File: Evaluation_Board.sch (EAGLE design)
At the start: 38 parts, among them IC1 MEGA32-A, IC2 FT232RL, IC3 317EMP, J1 DCJ0202, Q1 16 MHz

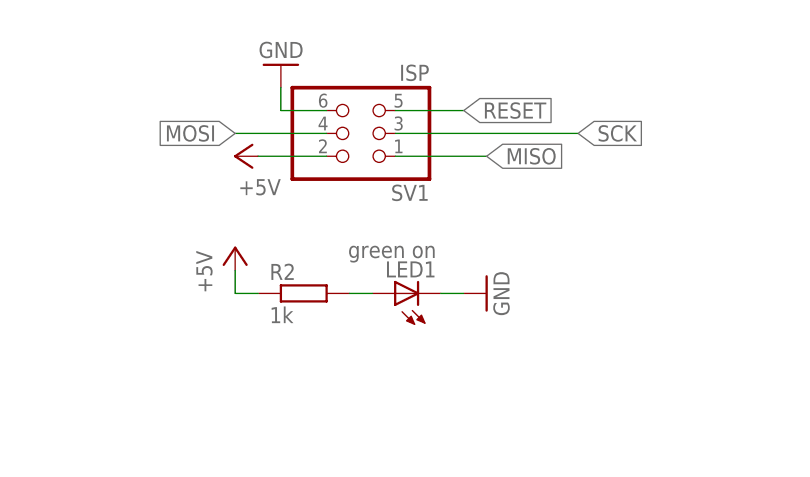
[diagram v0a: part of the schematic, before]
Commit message: Added name for ISP connector and placed a pin-one-marker on silk screen layer.
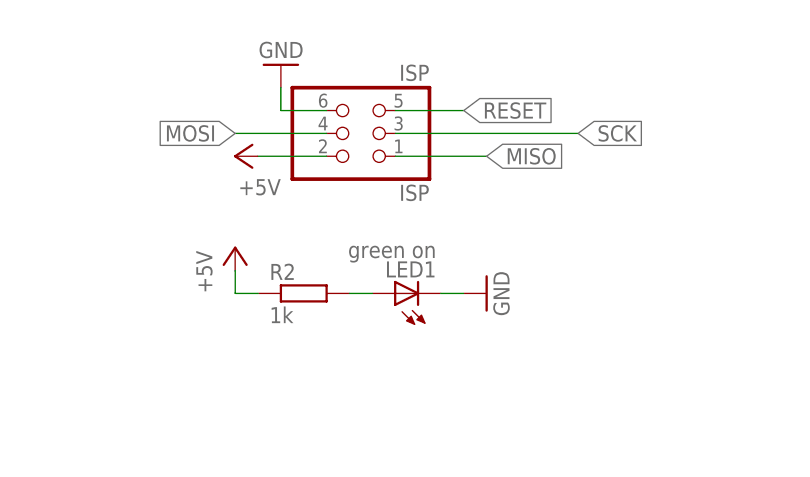
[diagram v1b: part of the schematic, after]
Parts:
- renumbered SV1 to ISP
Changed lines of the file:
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@@
 <part name="SUPPLY10" library="supply1" deviceset="GND" device=""/>
 <part name="X1" library="EmbeddedProjectsBauteile" deviceset="USB-B-BUCHSE-HORIZONTAL" device=""/>
-<part name="SV1" library="pinhead" deviceset="PINHD-2X3" device="" value="ISP"/>
+<part name="ISP" library="pinhead" deviceset="PINHD-2X3" device="" value="ISP"/>
 <part name="SV2" library="pinhead" deviceset="PINHD-1X8" device="" value="ADC"/>
 <part name="SUPPLY13" library="supply1" deviceset="+5V" device=""/>
@@
 <instance part="SUPPLY10" gate="1" x="292.1" y="223.52" rot="R90"/>
 <instance part="X1" gate="G$1" x="228.6" y="160.02" rot="R180"/>
-<instance part="SV1" gate="A" x="279.4" y="241.3" rot="R180"/>
+<instance part="ISP" gate="A" x="279.4" y="241.3" rot="R180"/>
 <instance part="SV2" gate="A" x="152.4" y="187.96"/>
 <instance part="SUPPLY13" gate="1" x="264.16" y="238.76" rot="R90"/>
@@
 <net name="RESET" class="0">
 <segment>
-<pinref part="SV1" gate="A" pin="5"/>
+<pinref part="ISP" gate="A" pin="5"/>
 <wire x1="281.94" y1="243.84" x2="289.56" y2="243.84" width="0.1524" layer="91"/>
 <label x="289.56" y="243.84" size="1.778" layer="95" xref="yes"/>
@@
 <net name="SCK" class="0">
 <segment>
-<pinref part="SV1" gate="A" pin="3"/>
+<pinref part="ISP" gate="A" pin="3"/>
 <wire x1="281.94" y1="241.3" x2="302.26" y2="241.3" width="0.1524" layer="91"/>
 <label x="302.26" y="241.3" size="1.778" layer="95" xref="yes"/>
@@
 <net name="MISO" class="0">
 <segment>
-<pinref part="SV1" gate="A" pin="1"/>
+<pinref part="ISP" gate="A" pin="1"/>
 <label x="292.1" y="238.76" size="1.778" layer="95" xref="yes"/>
 <wire x1="281.94" y1="238.76" x2="292.1" y2="238.76" width="0.1524" layer="91"/>
@@
 <net name="MOSI" class="0">
 <segment>
-<pinref part="SV1" gate="A" pin="4"/>
+<pinref part="ISP" gate="A" pin="4"/>
 <label x="264.16" y="241.3" size="1.778" layer="95" rot="R180" xref="yes"/>
 <wire x1="274.32" y1="241.3" x2="264.16" y2="241.3" width="0.1524" layer="91"/>
@@
 <segment>
 <pinref part="SUPPLY14" gate="1" pin="GND"/>
-<pinref part="SV1" gate="A" pin="6"/>
+<pinref part="ISP" gate="A" pin="6"/>
 <wire x1="269.24" y1="246.38" x2="269.24" y2="243.84" width="0.1524" layer="91"/>
 <wire x1="269.24" y1="243.84" x2="274.32" y2="243.84" width="0.1524" layer="91"/>
@@
 <net name="+5V" class="0">
 <segment>
-<pinref part="SV1" gate="A" pin="2"/>
+<pinref part="ISP" gate="A" pin="2"/>
 <pinref part="SUPPLY13" gate="1" pin="+5V"/>
 <wire x1="266.7" y1="238.76" x2="274.32" y2="238.76" width="0.1524" layer="91"/>
